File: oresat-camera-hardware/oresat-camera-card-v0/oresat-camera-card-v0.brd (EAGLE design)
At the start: 99.8 x 94.7 mm, 318 parts, among them J1 J-SAMTEC-TFM-120-X1-XXX-D-RA, J2 DM3BT-DSF-PEJS, J4 3-1734592-64-1734592-0, J8 2-1734592-0, Q1 DMP2240UDM, Q3 MIC842, Q4 MIC842, Q5 PMV45EN, Q6 MOSFET-PCH-SOT23-6, Q7 MOSFET-PCH-SOT23-6, Q8 PMV45EN, Q9 MMBT2907, U1 MAX7310ATE, U10 SN74LVC8T245MPWREPPW24-M, U11 RCLAMP0504FB, U12 RCLAMP0504FB, U13 TPS2051CDBVR, U14 TLVH431, U15 SN74LVC1G07DCK, U2 TPS62112, U3 MAX4211CETE, U4 TCAN330, U5 CLVCH16T245MDGGREP, U6 OSD3358-512M-BSM, U7 TCA9509DGKRDGK8-M, U9 TLV70028QDDCRQ1, Y1 24MHz

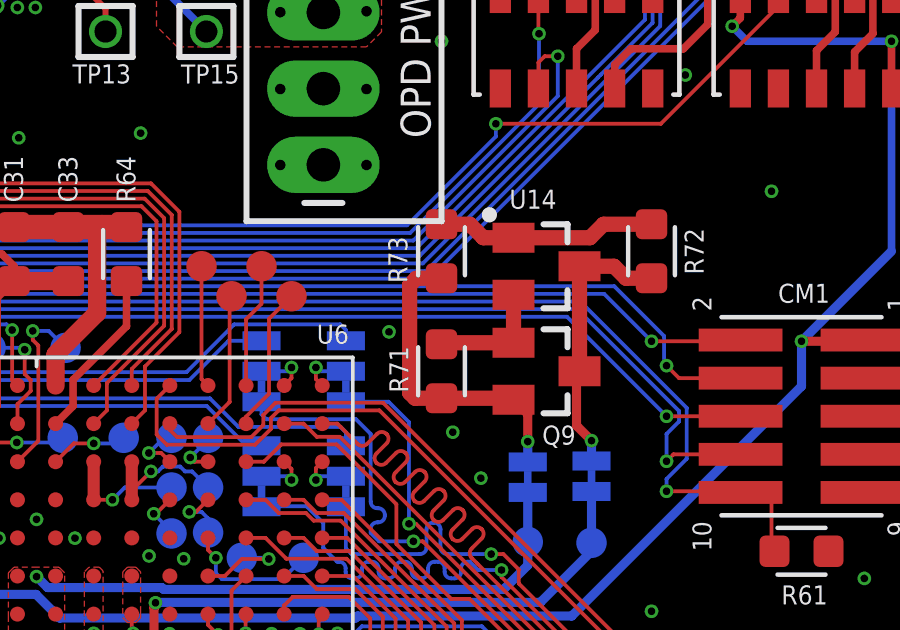
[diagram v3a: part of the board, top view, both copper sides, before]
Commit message: moved a resistor
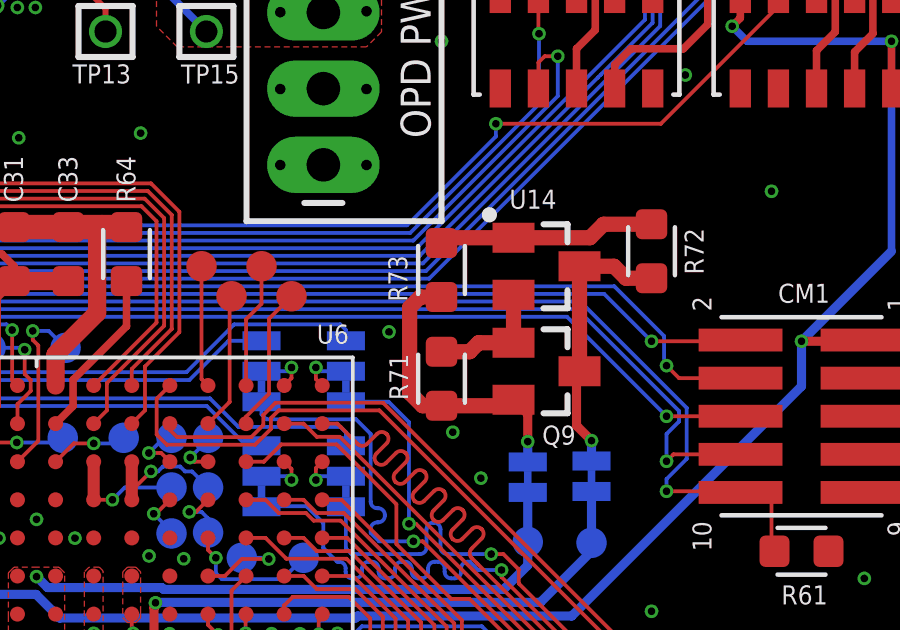
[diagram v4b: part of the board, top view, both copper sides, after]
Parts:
- moved R73 0.62 mm to (74.0, 62.4)
- moved R71 0.25 mm to (74.0, 58.8)
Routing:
- net N$20: track 10.6 -> 10.0 mm
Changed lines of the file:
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@@
 <layer number="14" name="Route14" color="1" fill="6" visible="no" active="no"/>
 <layer number="15" name="Route15" color="14" fill="1" visible="yes" active="yes"/>
-<layer number="16" name="Bottom" color="1" fill="1" visible="no" active="yes"/>
+<layer number="16" name="Bottom" color="1" fill="1" visible="yes" active="yes"/>
 <layer number="17" name="Pads" color="2" fill="1" visible="yes" active="yes"/>
 <layer number="18" name="Vias" color="2" fill="1" visible="yes" active="yes"/>
@@
 <layer number="20" name="Dimension" color="15" fill="1" visible="yes" active="yes"/>
 <layer number="21" name="tPlace" color="7" fill="1" visible="yes" active="yes"/>
-<layer number="22" name="bPlace" color="7" fill="1" visible="no" active="yes"/>
+<layer number="22" name="bPlace" color="7" fill="1" visible="yes" active="yes"/>
 <layer number="23" name="tOrigins" color="15" fill="1" visible="yes" active="yes"/>
 <layer number="24" name="bOrigins" color="15" fill="1" visible="yes" active="yes"/>
 <layer number="25" name="tNames" color="7" fill="1" visible="yes" active="yes"/>
-<layer number="26" name="bNames" color="7" fill="1" visible="no" active="yes"/>
+<layer number="26" name="bNames" color="7" fill="1" visible="yes" active="yes"/>
 <layer number="27" name="tValues" color="7" fill="1" visible="no" active="yes"/>
 <layer number="28" name="bValues" color="7" fill="1" visible="no" active="yes"/>
-<layer number="29" name="tStop" color="7" fill="3" visible="yes" active="yes"/>
+<layer number="29" name="tStop" color="7" fill="3" visible="no" active="yes"/>
 <layer number="30" name="bStop" color="7" fill="6" visible="no" active="yes"/>
 <layer number="31" name="tCream" color="7" fill="4" visible="no" active="yes"/>
@@
 <layer number="49" name="Reference" color="7" fill="1" visible="no" active="yes"/>
 <layer number="50" name="dxf" color="61" fill="1" visible="no" active="yes"/>
-<layer number="51" name="tDocu" color="7" fill="1" visible="no" active="yes"/>
-<layer number="52" name="bDocu" color="7" fill="1" visible="no" active="yes"/>
+<layer number="51" name="tDocu" color="7" fill="1" visible="yes" active="yes"/>
+<layer number="52" name="bDocu" color="7" fill="1" visible="yes" active="yes"/>
 <layer number="53" name="tGND_GNDA" color="7" fill="9" visible="no" active="no"/>
 <layer number="54" name="bGND_GNDA" color="1" fill="9" visible="no" active="no"/>
@@
 <attribute name="VALUE" x="79.405" y="63.77" size="0.635" layer="27" font="vector" ratio="20" rot="R270"/>
 </element>
-<element name="R73" library="oresat-rcl" package=".0603-A" value="10.0K" x="74" y="63" smashed="yes" rot="R270">
-<attribute name="NAME" x="72.8625" y="61.94375" size="0.635" layer="25" font="vector" ratio="20" rot="R90"/>
-<attribute name="NAME" x="74" y="63" size="0.3" layer="33" ratio="15" rot="R270" align="center"/>
-<attribute name="VALUE" x="72.25" y="64.4" size="0.8" layer="27" font="vector" ratio="15" rot="R270"/>
+<element name="R73" library="oresat-rcl" package=".0603-A" value="10.0K" x="74" y="62.375" smashed="yes" rot="R270">
+<attribute name="NAME" x="72.8625" y="61.31875" size="0.635" layer="25" font="vector" ratio="20" rot="R90"/>
+<attribute name="NAME" x="74" y="62.375" size="0.3" layer="33" ratio="15" rot="R270" align="center"/>
+<attribute name="VALUE" x="72.25" y="63.775" size="0.8" layer="27" font="vector" ratio="15" rot="R270"/>
 </element>
 <element name="R72" library="oresat-rcl" package=".0603-A" value="40.2K" x="81" y="63" smashed="yes" rot="R90">
@@
 <attribute name="VALUE" x="82.75" y="61.6" size="0.8" layer="27" font="vector" ratio="15" rot="R90"/>
 </element>
-<element name="R71" library="oresat-rcl" package=".0603-A" value="499" x="74" y="59" smashed="yes" rot="R270">
-<attribute name="NAME" x="72.89375" y="58.2875" size="0.635" layer="25" font="vector" ratio="20" rot="R90"/>
-<attribute name="NAME" x="74" y="59" size="0.3" layer="33" ratio="15" rot="R270" align="center"/>
-<attribute name="VALUE" x="72.25" y="60.4" size="0.8" layer="27" font="vector" ratio="15" rot="R270"/>
+<element name="R71" library="oresat-rcl" package=".0603-A" value="499" x="74" y="58.75" smashed="yes" rot="R270">
+<attribute name="NAME" x="72.89375" y="58.0375" size="0.635" layer="25" font="vector" ratio="20" rot="R90"/>
+<attribute name="NAME" x="74" y="58.75" size="0.3" layer="33" ratio="15" rot="R270" align="center"/>
+<attribute name="VALUE" x="72.25" y="60.15" size="0.8" layer="27" font="vector" ratio="15" rot="R270"/>
 </element>
 <element name="J9" library="SparkFun-Connectors" package="1X04_LONGPADS" value="" x="70.0625" y="73.5" smashed="yes" rot="R270">
@@
 <wire x1="79.4" y1="63.9" x2="81" y2="63.9" width="0.508" layer="1"/>
 <wire x1="78.95" y1="63.45" x2="79.4" y2="63.9" width="0.508" layer="1"/>
-<wire x1="76.4" y1="63.45" x2="75.39375" y2="63.45" width="0.508" layer="1"/>
-<wire x1="74.94375" y1="63.9" x2="74" y2="63.9" width="0.508" layer="1"/>
-<wire x1="75.39375" y1="63.45" x2="74.94375" y2="63.9" width="0.508" layer="1"/>
+<wire x1="74" y1="63.275" x2="74.175" y2="63.45" width="0.508" layer="1"/>
+<wire x1="76.4" y1="63.45" x2="74.175" y2="63.45" width="0.508" layer="1"/>
 </signal>
 <signal name="N$23">
@@
 <contactref element="R71" pad="1"/>
 <wire x1="76.4" y1="61.55" x2="76.4" y2="59.95" width="0.508" layer="1"/>
-<wire x1="76.4" y1="59.95" x2="74.05" y2="59.95" width="0.508" layer="1"/>
-<wire x1="74.05" y1="59.95" x2="74" y2="59.9" width="0.508" layer="1"/>
+<wire x1="76.4" y1="59.95" x2="75.2375" y2="59.95" width="0.508" layer="1"/>
+<wire x1="75.2375" y1="59.95" x2="74.9375" y2="59.65" width="0.508" layer="1"/>
+<wire x1="74.9375" y1="59.65" x2="74" y2="59.65" width="0.508" layer="1"/>
 </signal>
 <signal name="N$26">
@@
 <contactref element="Q9" pad="E"/>
 <contactref element="JP6" pad="2"/>
-<wire x1="74" y1="58.1" x2="76.35" y2="58.1" width="0.508" layer="1"/>
-<wire x1="76.35" y1="58.1" x2="76.4" y2="58.05" width="0.508" layer="1"/>
-<wire x1="74" y1="62.1" x2="73.1625" y2="62.1" width="0.508" layer="1"/>
-<wire x1="73.1625" y1="62.1" x2="72.9375" y2="61.875" width="0.508" layer="1"/>
-<wire x1="72.9375" y1="61.875" x2="72.9375" y2="58.28125" width="0.508" layer="1"/>
-<wire x1="73.11875" y1="58.1" x2="74" y2="58.1" width="0.508" layer="1"/>
-<wire x1="72.9375" y1="58.28125" x2="73.11875" y2="58.1" width="0.508" layer="1"/>
+<wire x1="76.4" y1="58.05" x2="76.2" y2="57.85" width="0.508" layer="1"/>
+<wire x1="76.2" y1="57.85" x2="74" y2="57.85" width="0.508" layer="1"/>
+<wire x1="74" y1="61.475" x2="73.2875" y2="61.475" width="0.508" layer="1"/>
+<wire x1="73.2875" y1="61.475" x2="72.9375" y2="61.125" width="0.508" layer="1"/>
+<wire x1="72.9375" y1="61.125" x2="72.9375" y2="58.28125" width="0.508" layer="1"/>
+<wire x1="73.36875" y1="57.85" x2="74" y2="57.85" width="0.508" layer="1"/>
+<wire x1="72.9375" y1="58.28125" x2="73.36875" y2="57.85" width="0.508" layer="1"/>
 <wire x1="76.875" y1="55.97675" x2="76.875" y2="56.65625" width="0.3048" layer="16"/>
 <via x="76.875" y="56.65625" extent="1-16" drill="0.254"/>

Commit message: moved chip a bit
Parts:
- C31, C33, C34: device oresat-rcl:.0603-A-NOSILK -> oresat-rcl:.0603-A
- moved C17 0.44 mm to (17.0, 51.9)
- moved U7 0.31 mm to (17.0, 47.8)
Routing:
- net 2.8V: track 58.3 -> 58.8 mm

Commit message: last minute changes
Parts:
- added TP151: TEST-POINT3X4, SparkFun-Connectors:PAD.03X.04
- added U$2: (no value), psas-logo:PSAS_LOGO_10X10
- moved D4 0.56 mm to (51.0, 5.88)
- moved D5 0.56 mm to (53.0, 5.88)
- moved D6 0.56 mm to (55.0, 5.88)
- moved D7 0.56 mm to (57.0, 5.88)
- moved D8 0.56 mm to (49.0, 5.88)
- moved R49 0.12 mm to (51.0, 8.94)
- moved R50 0.12 mm to (53.0, 8.94)
- moved R51 0.12 mm to (55.0, 8.94)
- moved R52 0.12 mm to (57.0, 8.94)
- moved R70 0.12 mm to (49.0, 8.94)
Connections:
- net N$3: now also TP151.P$1
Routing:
- net N$3: track 1.27 -> 3.00 mm, vias 0 -> 1
- net GND: vias 268 -> 269
